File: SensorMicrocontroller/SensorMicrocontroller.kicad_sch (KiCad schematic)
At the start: 10 parts, among them J1 JST B6B-PH-SM4-TB, J2 JST B4B-PH-SM4-TB, J3 JST B4B-PH-SM4-TB, J4 JST B4B-PH-SM4-TB, J5 JST B4B-PH-SM4-TB, U1 SC0915, U2 ADS1115IDGS

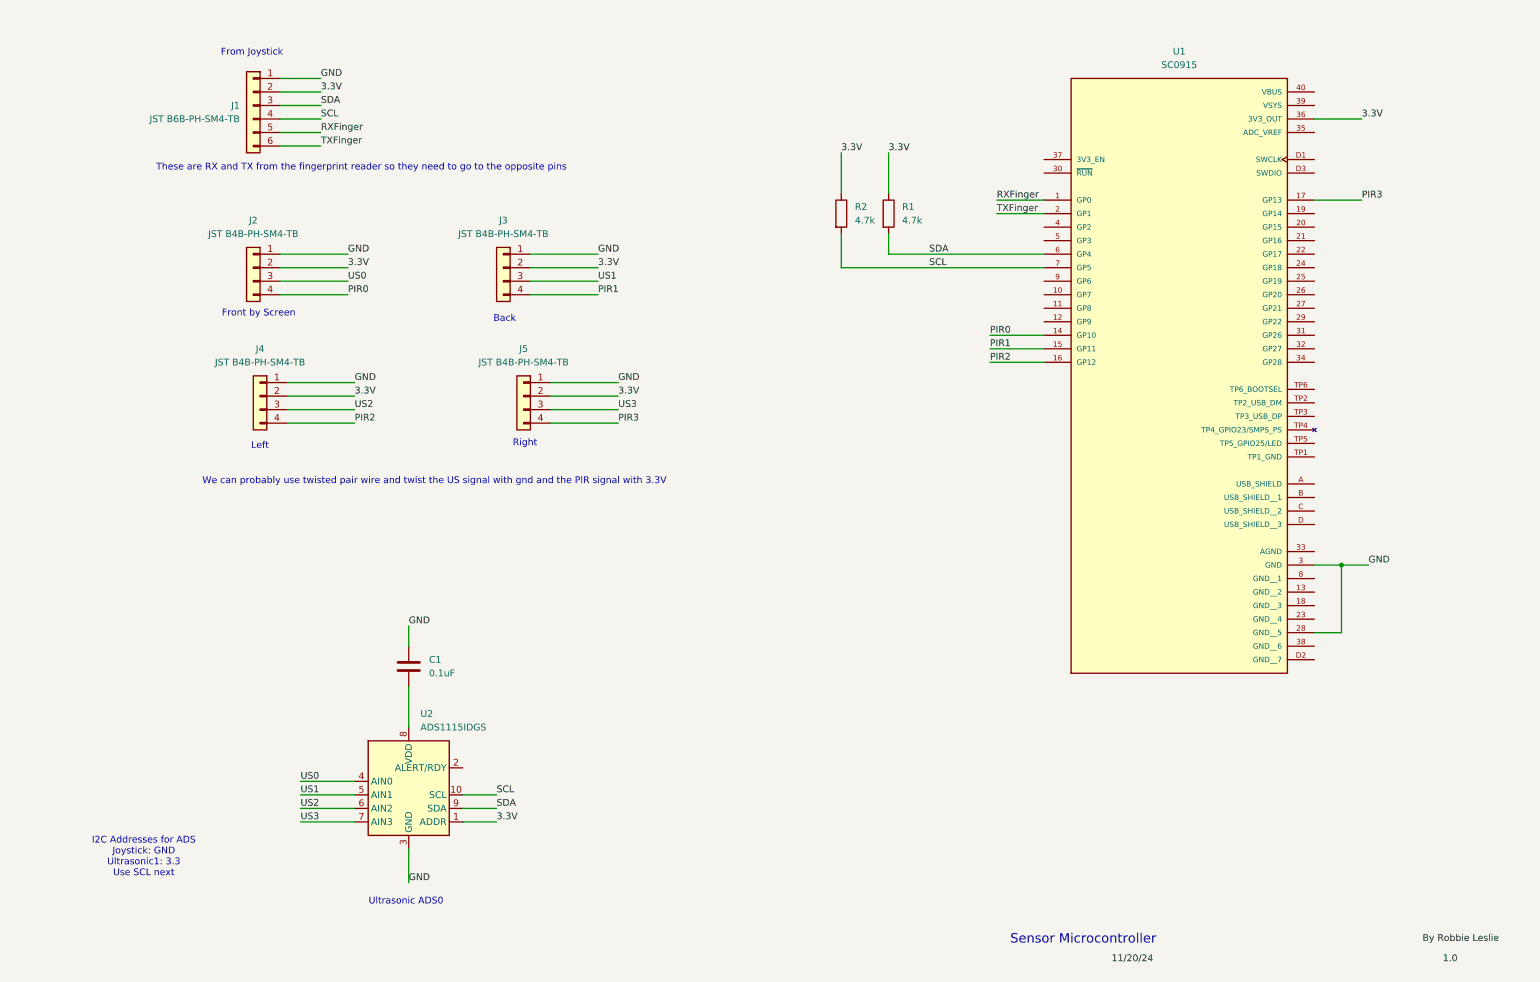
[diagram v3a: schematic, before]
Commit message: Added PWM fan conncectors
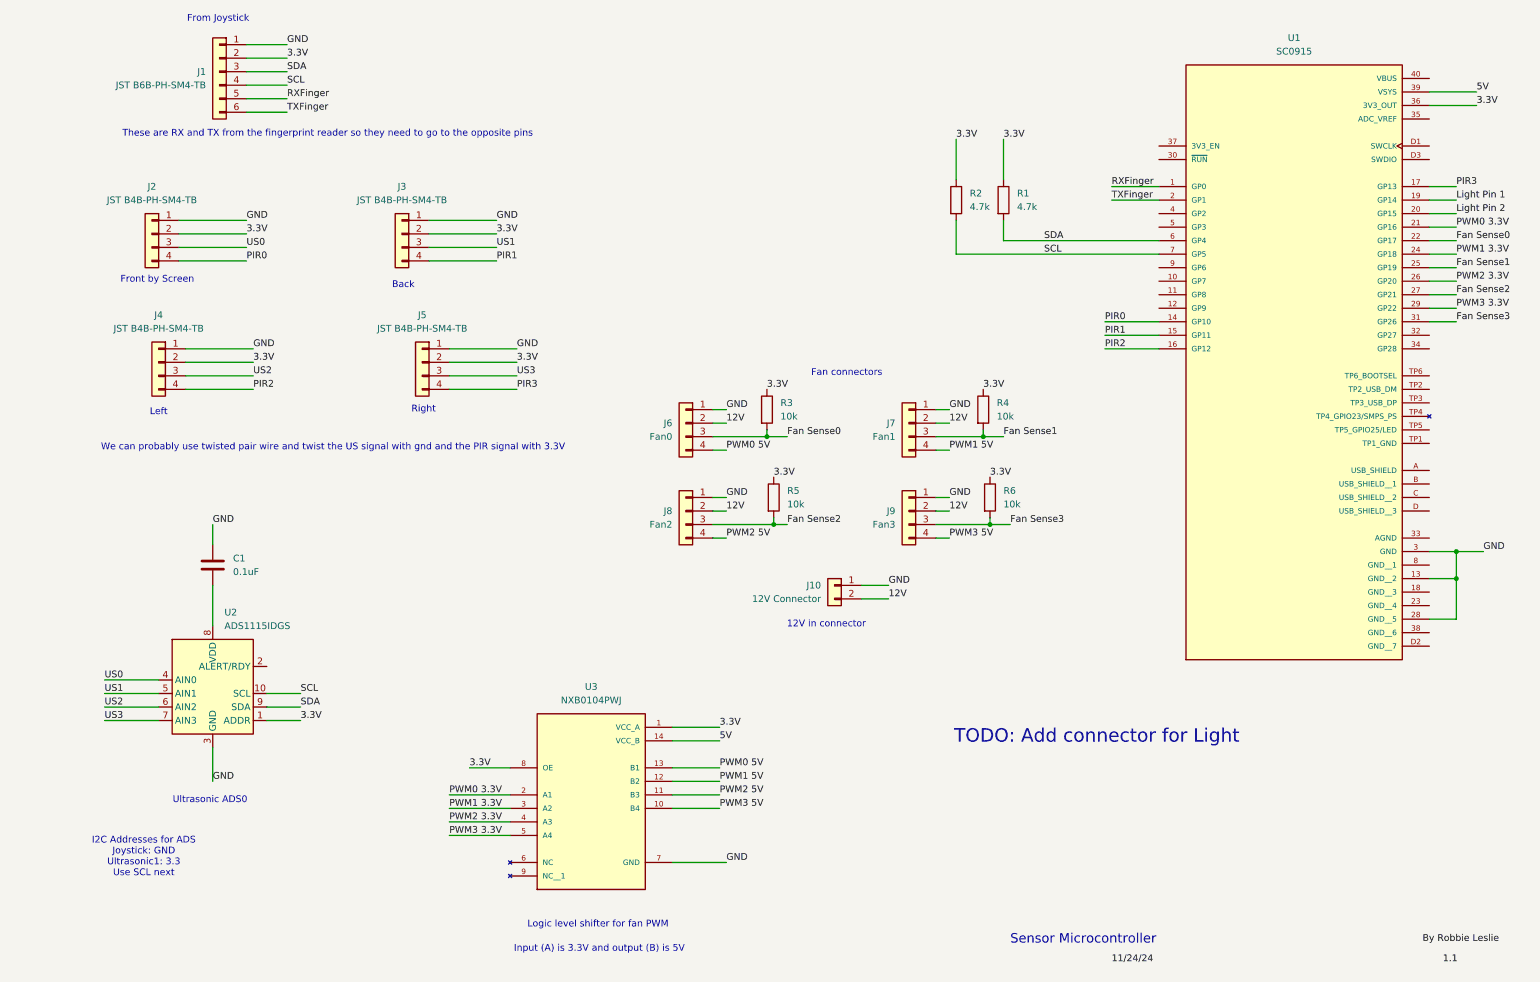
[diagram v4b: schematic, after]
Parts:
- added J10: 12V Connector, Connector_JST:JST_PH_B2B-PH-SM4-TB_1x02-1MP_P2.00mm_Vertical, symbol Connector_Generic:Conn_01x02
- added J6: Fan0, Connector_Molex:Molex_KK-254_AE-6410-04A_1x04_P2.54mm_Vertical, symbol Connector_Generic:Conn_01x04
- added J7: Fan1, Connector_Molex:Molex_KK-254_AE-6410-04A_1x04_P2.54mm_Vertical, symbol Connector_Generic:Conn_01x04
- added J8: Fan2, Connector_Molex:Molex_KK-254_AE-6410-04A_1x04_P2.54mm_Vertical, symbol Connector_Generic:Conn_01x04
- added J9: Fan3, Connector_Molex:Molex_KK-254_AE-6410-04A_1x04_P2.54mm_Vertical, symbol Connector_Generic:Conn_01x04
- added R3, R4, R5, R6: 10k, Resistor_SMD:R_0805_2012Metric, symbol Device:R
- added U3: NXB0104PWJ, Package_SO:TSSOP-14_4.4x5mm_P0.65mm, symbol NXB0104PWJ:NXB0104PWJ
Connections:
- net 3.3V: now also R3.1, R4.1, R5.1, R6.1, U3.1 (VCC_A), U3.8 (OE)
- net GND: now also U1.13 (GND__2), J10.1 (Pin_1), J6.1 (Pin_1), J7.1 (Pin_1), J8.1 (Pin_1), J9.1 (Pin_1), U3.7 (GND)
- net Light Pin 1: now reaches U1.19 (GP14)
- net Light Pin 2: now reaches U1.20 (GP15)
- net PWM0 3.3V: now reaches U1.21 (GP16)
- net PWM0 3.3V: now also U3.2 (A1)
- net Fan Sense0: now reaches U1.22 (GP17)
- net Fan Sense0: now also J6.3 (Pin_3), R3.2
- net PWM1 3.3V: now reaches U1.24 (GP18)
- net PWM1 3.3V: now also U3.3 (A2)
- net Fan Sense1: now reaches U1.25 (GP19)
- net Fan Sense1: now also J7.3 (Pin_3), R4.2
- net PWM2 3.3V: now reaches U1.26 (GP20)
- net PWM2 3.3V: now also U3.4 (A3)
- net Fan Sense2: now reaches U1.27 (GP21)
- net Fan Sense2: now also J8.3 (Pin_3), R5.2
- net PWM3 3.3V: now reaches U1.29 (GP22)
- net PWM3 3.3V: now also U3.5 (A4)
- net Fan Sense3: now reaches U1.31 (GP26)
- net Fan Sense3: now also J9.3 (Pin_3), R6.2
- net 5V: now reaches U1.39 (VSYS)
- net 5V: now also U3.14 (VCC_B)
- new net 12V: J10.2 (Pin_2), J6.2 (Pin_2), J7.2 (Pin_2), J8.2 (Pin_2), J9.2 (Pin_2)
- new net PWM0 5V: J6.4 (Pin_4), U3.13 (B1)
- new net PWM1 5V: J7.4 (Pin_4), U3.12 (B2)
- new net PWM2 5V: J8.4 (Pin_4), U3.11 (B3)
- new net PWM3 5V: J9.4 (Pin_4), U3.10 (B4)
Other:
- note added: "12V in connector"
- note added: "Fan connectors"
- note added: "Input (A) is 3.3V and output (B) is 5V"
- note added: "Logic level shifter for fan PWM"
- note added: "TODO: Add connector for Light"
- moved on the sheet: C1, J1, J2, J3, J4, J5, R1, R2, U1, U2

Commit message: Updated footprint for fan headers
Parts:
- J6, J7, J8, J9: footprint Connector_Molex:Molex_KK-254_AE-6410-04A_1x04_P2.54mm_Vertical -> Connector:FanPinHeader_1x04_P2.54mm_Vertical
- U1: footprint SC0915:MODULE_SC0915 -> Footprints:pico
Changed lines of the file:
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@@
 			)
 		)
-		(property "Footprint" "Connector_Molex:Molex_KK-254_AE-6410-04A_1x04_P2.54mm_Vertical"
+		(property "Footprint" "Connector:FanPinHeader_1x04_P2.54mm_Vertical"
 			(at 127 109.22 0)
 			(effects
@@
 			)
 		)
-		(property "Footprint" "Connector_Molex:Molex_KK-254_AE-6410-04A_1x04_P2.54mm_Vertical"
+		(property "Footprint" "Connector:FanPinHeader_1x04_P2.54mm_Vertical"
 			(at 168.91 109.22 0)
 			(effects
@@
 			)
 		)
-		(property "Footprint" "Connector_Molex:Molex_KK-254_AE-6410-04A_1x04_P2.54mm_Vertical"
+		(property "Footprint" "Connector:FanPinHeader_1x04_P2.54mm_Vertical"
 			(at 168.91 92.71 0)
 			(effects
@@
 			)
 		)
-		(property "Footprint" "Connector_Molex:Molex_KK-254_AE-6410-04A_1x04_P2.54mm_Vertical"
+		(property "Footprint" "Connector:FanPinHeader_1x04_P2.54mm_Vertical"
 			(at 127 92.71 0)
 			(effects
@@
 			)
 		)
-		(property "Footprint" "SC0915:MODULE_SC0915"
+		(property "Footprint" "Footprints:pico"
 			(at 241.3 68.58 0)
 			(effects

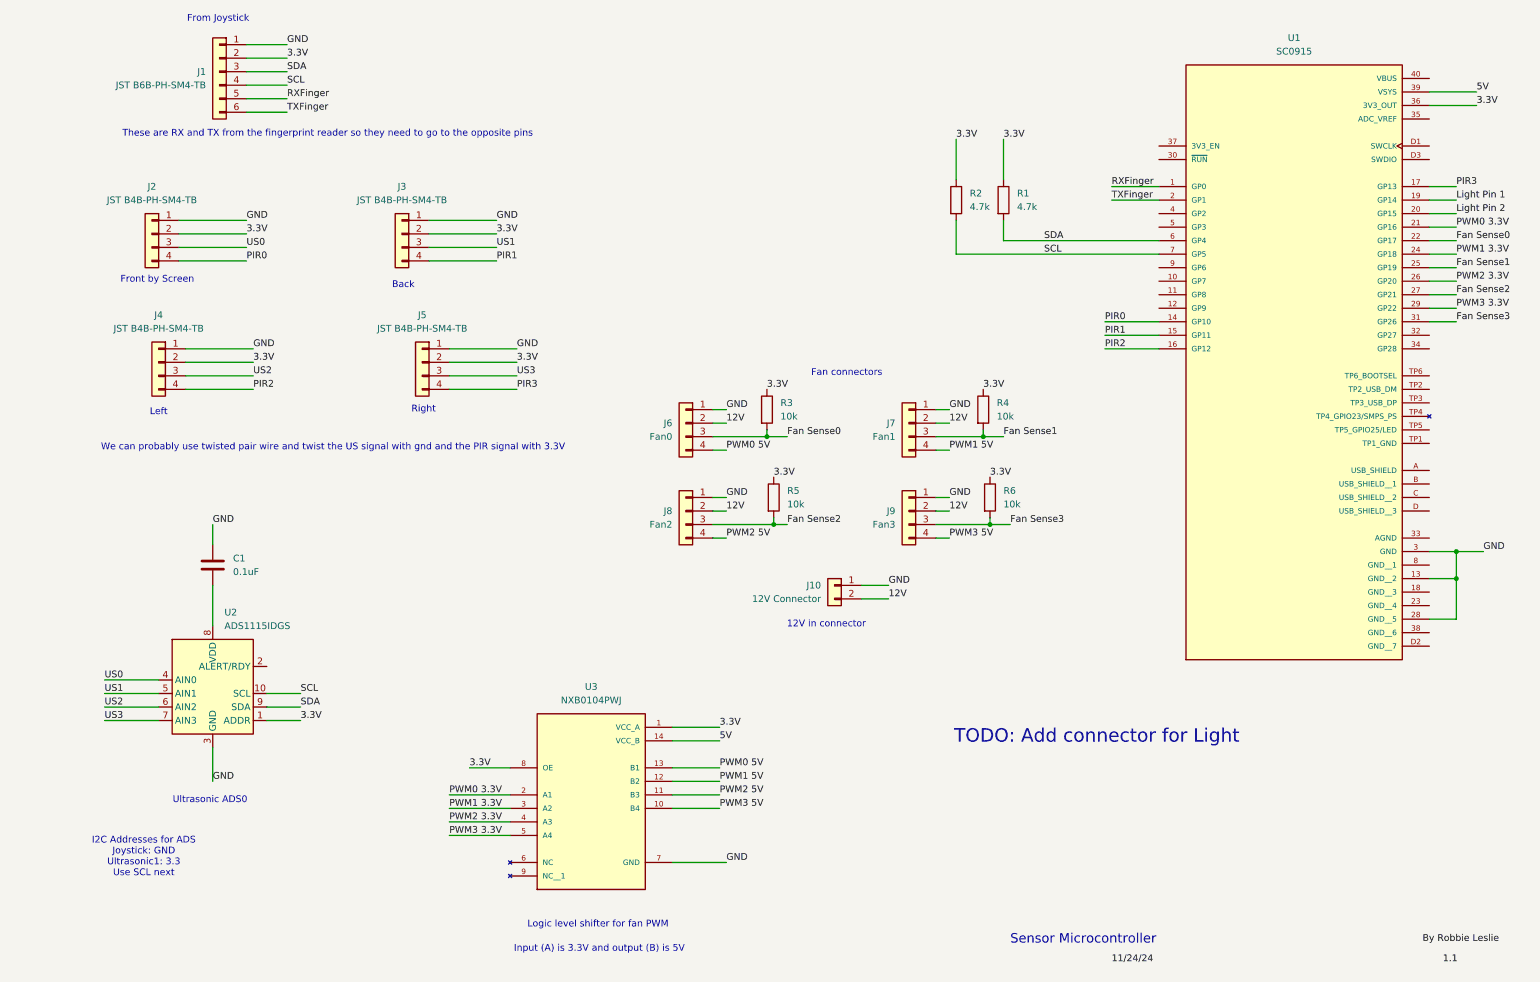
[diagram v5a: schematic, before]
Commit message: Changed logic level shifter for opto-isolator and started work on fan transistors
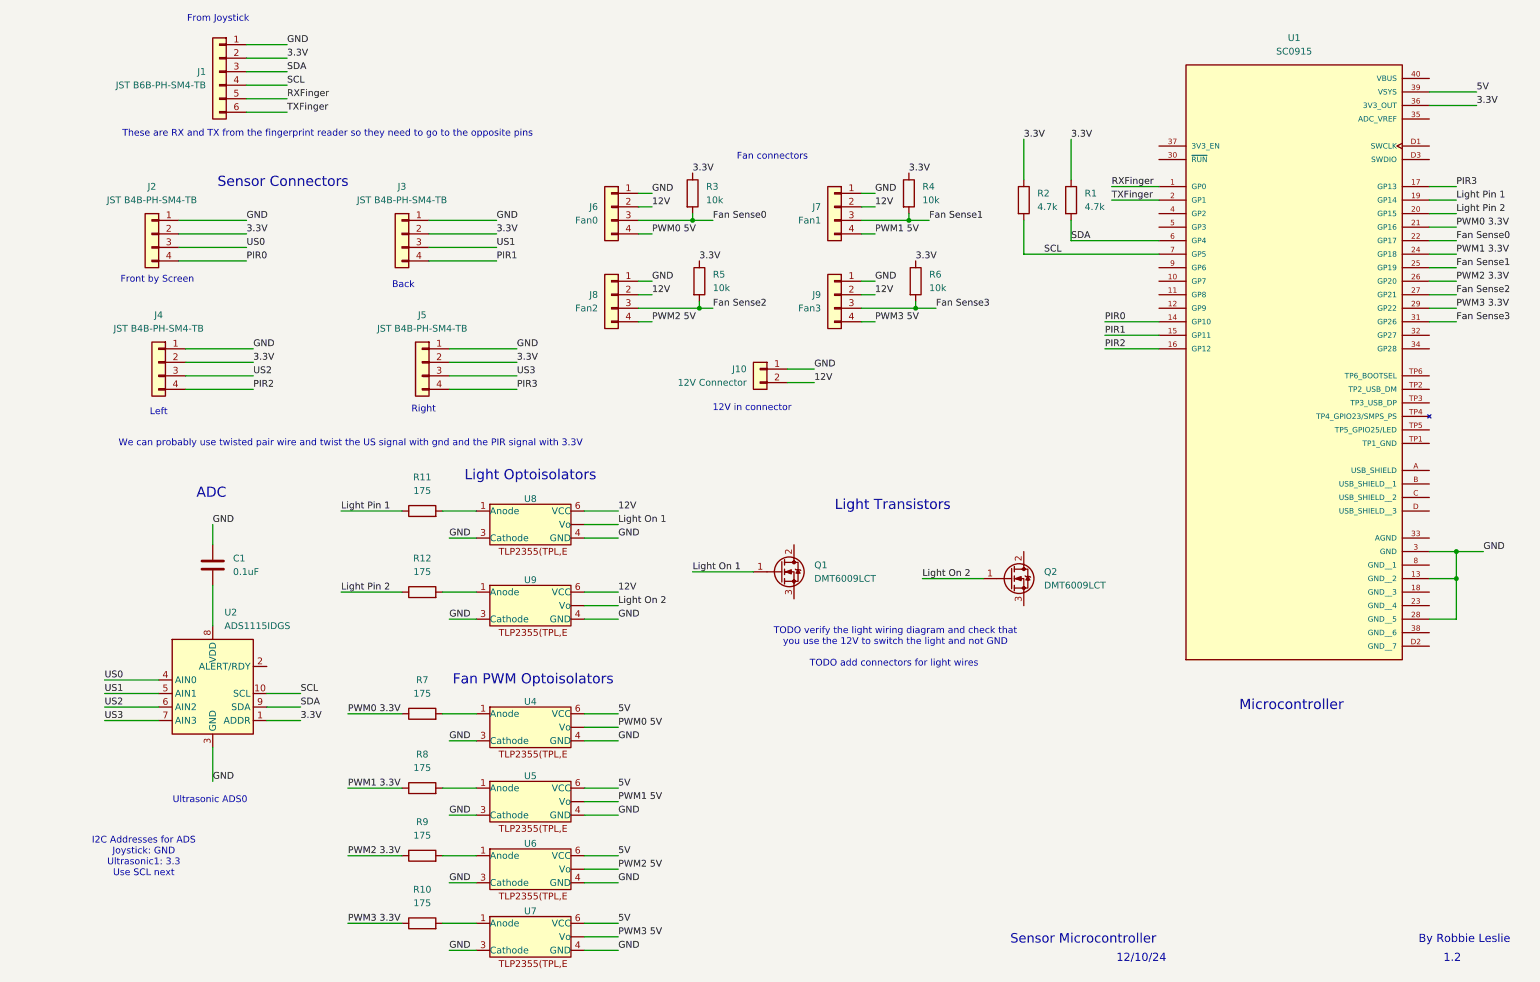
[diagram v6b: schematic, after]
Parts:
- removed U3: NXB0104PWJ, Package_SO:TSSOP-14_4.4x5mm_P0.65mm, symbol NXB0104PWJ:NXB0104PWJ
- added Q1, Q2: DMT6009LCT, Package_TO_SOT_THT:TO-220-3_Horizontal_TabUp, symbol Device:Q_NMOS_GDS
- added R10, R11, R12, R7, R8, R9: 175, Resistor_SMD:R_0805_2012Metric, symbol Device:R
- added U4, U5, U6, U7, U8, U9: ~, Package_SO:SO-5-6_4.55x3.7mm_P1.27mm, symbol OptoIsolators:TLP2355(TPL,E
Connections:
- net 12V: now also U8.6 (VCC), U9.6 (VCC)
- net 5V: now also U4.6 (VCC), U5.6 (VCC), U6.6 (VCC), U7.6 (VCC)
- net GND: now also U4.3 (Cathode), U4.4 (GND), U5.3 (Cathode), U5.4 (GND), U6.3 (Cathode), U6.4 (GND), U7.3 (Cathode), U7.4 (GND), U8.3 (Cathode), U8.4 (GND), U9.3 (Cathode), U9.4 (GND)
- net Light Pin 1: now also R11.1
- net Light Pin 2: now also R12.1
- net PWM0 3.3V: now also R7.1
- net PWM0 5V: now also U4. (Vo)
- net PWM1 3.3V: now also R8.1
- net PWM1 5V: now also U5. (Vo)
- net PWM2 3.3V: now also R9.1
- net PWM2 5V: now also U6. (Vo)
- net PWM3 3.3V: now also R10.1
- net PWM3 5V: now also U7. (Vo)
- new net: R9.2, U6.1 (Anode)
- new net: R10.2, U7.1 (Anode)
- new net: R11.2, U8.1 (Anode)
- new net: R7.2, U4.1 (Anode)
- new net: R12.2, U9.1 (Anode)
- new net: R8.2, U5.1 (Anode)
- new net Light On 1: Q1.1 (G), U8. (Vo)
- new net Light On 2: Q2.1 (G), U9. (Vo)
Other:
- note added: "1.2"
- note added: "12/10/24"
- note added: "ADC"
- note added: "By Robbie Leslie"
- note added: "Fan PWM Optoisolators"
- note added: "Light Optoisolators"
- note added: "Light Transistors"
- note added: "Microcontroller"
- note added: "Sensor Connectors"
- note added: "TODO add connectors for light wires"
- note added: "TODO verify the light wiring diagram and check that you use the 12V to switch the light and not GND"
- note removed: "Input (A) is 3.3V and output (B) is 5V"
- note removed: "Logic level shifter for fan PWM"
- note removed: "TODO: Add connector for Light"
- moved on the sheet: J10, J6, J7, J8, J9, R1, R2, R3, R4, R5, R6

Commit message: Initial wiring for light
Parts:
- added F1: Fuse, symbol Device:Fuse
- added J11: Light Connector, Connector:FanPinHeader_1x04_P2.54mm_Vertical, symbol Connector_Generic:Conn_01x04
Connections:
- net 12V: now also F1.1
- net GND: now also Q2.3 (S), J11.3 (Pin_3)
- net Light Red Wire: now reaches Q1.2 (D)
- net Light Red Wire: now also Q2.2 (D), J11.1 (Pin_1)
- net Light Blue Wire: now reaches Q1.3 (S)
- net Light Blue Wire: now also J11.2 (Pin_2)
- new net Light White Wire: F1.2, J11.4 (Pin_4)
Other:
- note added: "1.3"
- note added: "1/8/25"
- note added: "TODO select the fuse on white wire"
- note added: "TODO swap connectors for light wires to JST EH connector"
- note removed: "1.2"
- note removed: "12/10/24"
- note removed: "TODO add connectors for light wires"

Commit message: Swapped light connector for JST EH and selected fuse
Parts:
- F1: footprint (none) -> Fuse:Fuse_0805_2012Metric
- J11: footprint Connector:FanPinHeader_1x04_P2.54mm_Vertical -> Connector_JST:JST_EH_B4B-EH-A_1x04_P2.50mm_Vertical
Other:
- note added: "1/9/25"
- note removed: "1/8/25"
- note removed: "TODO select the fuse on white wire"
- note removed: "TODO swap connectors for light wires to JST EH connector"
- note removed: "TODO verify the light wiring diagram and check that you use the 12V to switch the light and not GND"
